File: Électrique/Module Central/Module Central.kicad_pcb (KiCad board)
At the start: 2 copper layers, 48.2 x 45.8 mm, 48 parts, among them J101 2.1mm X 5.5mm Barrel Connector, J102 Prog, J103 Conn_Coaxial, J201 USB_B_Mini, J301 Borne 0, J302 Borne 1, J303 Borne 2, J304 Borne 3, U101 LM2937xMP, U102 ATmega328P-AU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

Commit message: Ajout DEL témoin
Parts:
- added D105: TA, Diode_SMD:D_0805_2012Metric, F.Cu at (131.0, 44.8)
- added R106: 330, Resistor_SMD:R_0805_2012Metric, B.Cu at (131.8, 44.8)
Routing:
- net 5V: track 177.9 -> 182.5 mm
- net Net-(D105-Pad1): track 0.00 -> 4.53 mm, vias 0 -> 1

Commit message: Modification PCB prete à faire
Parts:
- added R201: 10K, Resistor_SMD:R_0805_2012Metric, F.Cu at (164.8, 35.5)
- added U104: FXMA108, Package_DFN_QFN:WQFN-20-1EP_2.5x4.5mm_P0.5mm_EP1x2.9mm, F.Cu at (149.2, 37.5)
- C203: value 0.01 -> 0.1
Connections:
- R102 pad 2: GND -> Net-(R102-Pad2)
- R103 pad 2: GND -> Net-(R103-Pad2)
- R104 pad 2: GND -> Net-(R104-Pad2)
- R105 pad 2: GND -> Net-(R105-Pad2)
- R106 pad 2: GND -> Net-(R106-Pad2)
- U102 pad 23: RX -> Net-(U102-Pad23)
- U102 pad 24: TX -> Net-(U102-Pad24)
- U102 pad 30: Net-(U102-Pad30) -> RX
- U102 pad 31: Net-(U102-Pad31) -> TX
- U102 pad 32: /D2 -> Net-(U102-Pad32)
- U103 pad 14: /D2 -> Net-(U103-Pad14)
- U103 pad 2: Net-(JP101-Pad2) -> Net-(U103-Pad2)
- U103 pad 3: Net-(JP102-Pad2) -> Net-(U103-Pad3)
- U103 pad 5: /D10 -> Net-(U103-Pad5)
- U103 pad 6: /D9 -> Net-(U103-Pad6)
- U201 pad 15: Net-(C201-Pad1) -> Net-(J201-Pad3)
- U201 pad 16: Net-(C202-Pad1) -> Net-(J201-Pad2)

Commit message: PCB modifié
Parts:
- removed C201, C202: 47p, Capacitor_SMD:C_0805_2012Metric
- removed the R201 at (125.2, 41.0)
- removed R202: 20, Resistor_SMD:R_0805_2012Metric
- R201, U104: moved to B.Cu
- moved R201 63.4 mm to (105.0, 56.8)
- moved U104 33.7 mm to (122.5, 58.0), turned to 90 degrees
- moved J103 0.50 mm to (108.2, 36.0)
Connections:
- R102 pad 2: Net-(R102-Pad2) -> GND
- R103 pad 2: Net-(R103-Pad2) -> GND
- R104 pad 2: Net-(R104-Pad2) -> GND
- R105 pad 2: Net-(R105-Pad2) -> GND
- R106 pad 2: Net-(R106-Pad2) -> GND
- U103 pad 4: /SCK_D13 -> Net-(U103-Pad4)
- U104 pad 14: Net-(U104-Pad14) -> Net-(U103-Pad4)
- U104 pad 7: Net-(U104-Pad7) -> /SCK_D13
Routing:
- net Net-(U103-Pad14): track 0.00 -> 22.2 mm, vias 0 -> 3
- net /D2: track 16.2 -> 0.00 mm
- net Net-(J201-Pad2): track 4.80 -> 20.1 mm
- net Net-(C202-Pad1): track 14.9 -> 0.00 mm
- net /D9: track 26.9 -> 12.1 mm, vias 2 -> 1
- net Net-(JP102-Pad2): track 20.8 -> 34.5 mm, vias 2 -> 3
- net Net-(U102-Pad32): track 0.00 -> 13.2 mm, vias 0 -> 3
- net Net-(U103-Pad6): track 0.00 -> 12.9 mm, vias 0 -> 1
- net GND: track 111.6 -> 124.1 mm, vias 11 -> 14
- net /D10: track 24.4 -> 12.4 mm, vias 2 -> 1
- net 5V: track 182.5 -> 193.6 mm
- net Net-(U103-Pad5): track 0.00 -> 10.5 mm, vias 0 -> 1
- net Net-(J201-Pad3): track 9.58 -> 19.9 mm
- net Net-(C201-Pad1): track 10.00 -> 0.00 mm
- net RX: track 11.0 -> 2.66 mm
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
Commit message: Modif PCB en cours
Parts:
- added JP103: Jumper, Connector_PinSocket_2.54mm:PinSocket_1x02_P2.54mm_Vertical, F.Cu at (147.2, 57.0)
- added JP104: Jumper, Connector_PinSocket_2.54mm:PinSocket_1x02_P2.54mm_Vertical, F.Cu at (151.8, 57.0)
- added R107: 1K, Resistor_SMD:R_0805_2012Metric, F.Cu at (147.1, 63.3)
- added R108: 1K, Resistor_SMD:R_0805_2012Metric, F.Cu at (151.5, 63.3)
- added U105: TXB0104RGY, Package_DFN_QFN:Texas_S-PVQFN-N14, B.Cu at (117.8, 58.0)
- U104: value FXMA108 -> TXB0104RGY; footprint Package_DFN_QFN:WQFN-20-1EP_2.5x4.5mm_P0.5mm_EP1x2.9mm -> Package_DFN_QFN:Texas_S-PVQFN-N14
- moved U104 0.25 mm to (122.8, 58.0), turned to 270 degrees
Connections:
- U104 pad 1: 5V -> 3V3
- U104 pad 10: GND -> Net-(U102-Pad32)
- U104 pad 11: GND -> Net-(JP101-Pad2)
- U104 pad 12: Net-(U104-Pad12) -> Net-(JP102-Pad2)
- U104 pad 13: Net-(U104-Pad13) -> /SCK_D13
- U104 pad 14: Net-(U103-Pad4) -> 5V
- U104 pad 15: Net-(U103-Pad6) -> GND
- U104 pad 2: Net-(U102-Pad32) -> Net-(U103-Pad4)
- U104 pad 3: Net-(JP101-Pad2) -> Net-(U103-Pad3)
- U104 pad 4: Net-(JP102-Pad2) -> Net-(U103-Pad2)
- U104 pad 5: /D10 -> Net-(U103-Pad14)
- U104 pad 6: /D9 -> Net-(U104-Pad6)
- U104 pad 7: /SCK_D13 -> GND
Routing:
- net Net-(U102-Pad32): track 13.2 -> 0.00 mm, vias 3 -> 0
- net DTR: track 31.3 -> 37.5 mm
- net Net-(U103-Pad14): track 22.2 -> 27.5 mm
- net Net-(JP102-Pad2): track 34.5 -> 30.7 mm
- net Net-(U103-Pad5): track 10.5 -> 13.8 mm
- net 3V3: track 45.8 -> 42.6 mm
- net GND: track 124.1 -> 121.8 mm, vias 14 -> 13
- net Net-(U103-Pad6): track 12.9 -> 14.9 mm
- net Net-(U103-Pad2): track 8.26 -> 10.0 mm
- net Net-(R203-Pad2): track 10.9 -> 12.6 mm
- net TX: track 16.5 -> 18.1 mm
- net 5V: track 193.6 -> 192.2 mm
- net /MOSI_D11: track 37.7 -> 39.0 mm
- net /D9: track 12.1 -> 13.3 mm
- net Net-(JP101-Pad2): track 26.4 -> 25.2 mm
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
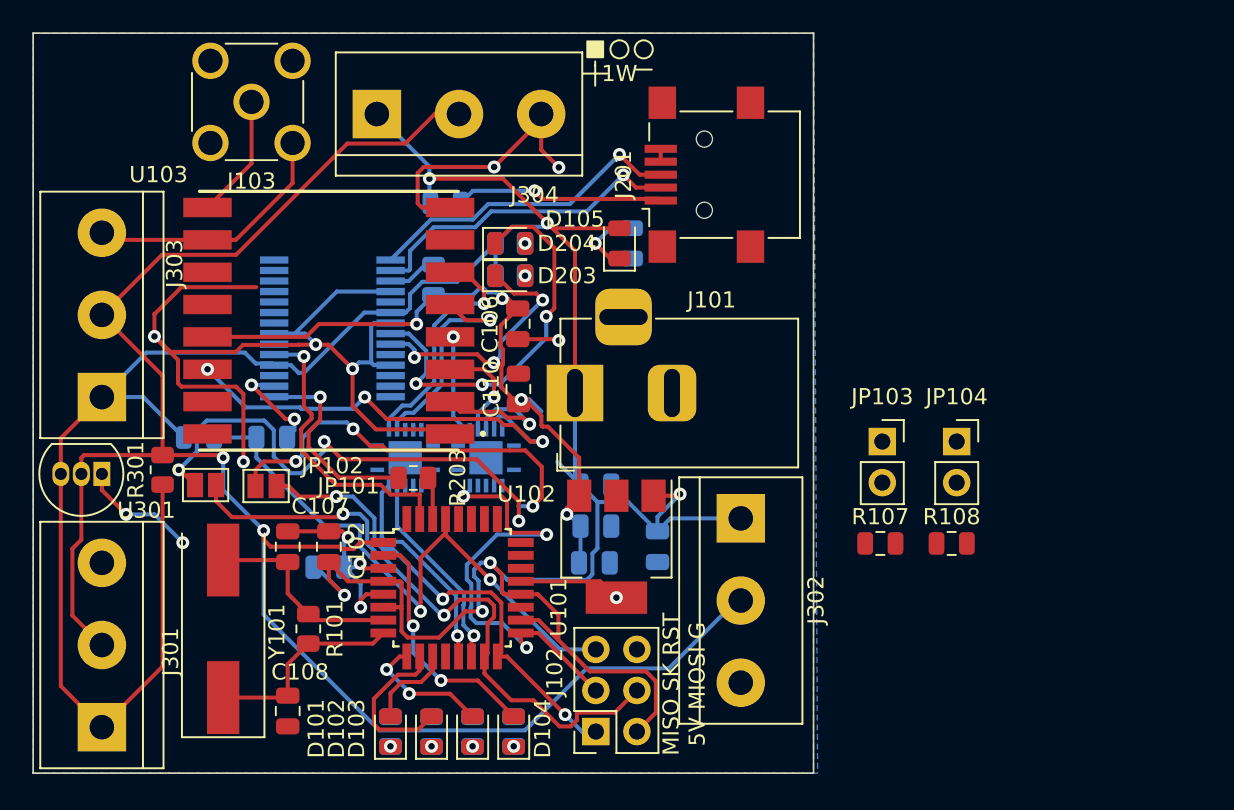
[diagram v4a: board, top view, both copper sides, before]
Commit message: PCB Avec 2x 4Channel LevelShifters
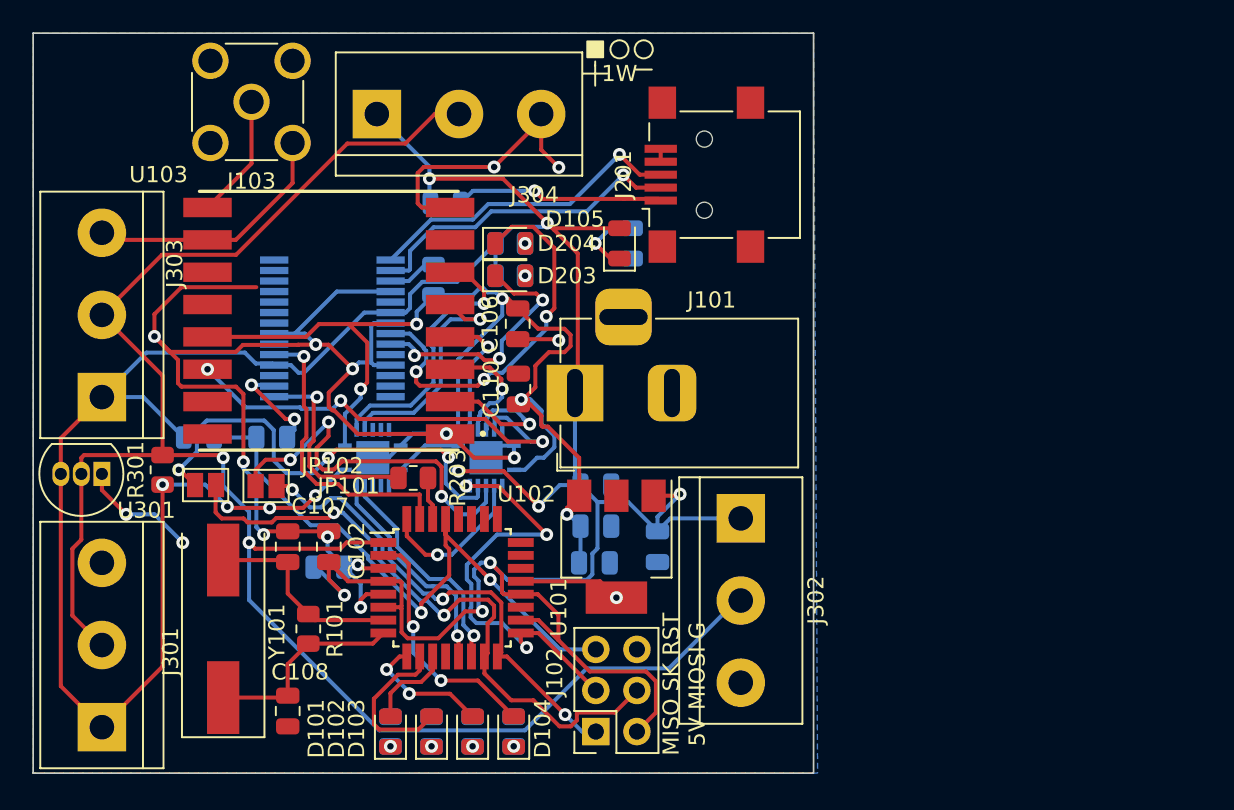
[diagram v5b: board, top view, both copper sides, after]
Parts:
- removed JP103, JP104: Jumper, Connector_PinSocket_2.54mm:PinSocket_1x02_P2.54mm_Vertical
- removed R107, R108: 1K, Resistor_SMD:R_0805_2012Metric
- moved U105 2.00 mm to (115.8, 58.0)
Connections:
- U104 pad 8: Net-(JP104-Pad1) -> 3V3
- U105 pad 8: Net-(JP103-Pad1) -> 3V3
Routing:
- net 3V3: track 42.6 -> 76.3 mm, vias 4 -> 5
- net GND: track 121.8 -> 142.3 mm, vias 13 -> 16
- net 5V: track 192.2 -> 212.3 mm, vias 6 -> 12
- net Net-(U102-Pad32): track 0.00 -> 9.67 mm, vias 0 -> 1
- net Net-(JP102-Pad2): track 30.7 -> 28.1 mm
- net Net-(U103-Pad6): track 14.9 -> 17.0 mm
- net Net-(U103-Pad4): track 6.30 -> 8.18 mm
- net /D10: track 12.6 -> 14.2 mm
- net Net-(JP101-Pad2): track 25.2 -> 24.2 mm
- net /SCK_D13: track 28.1 -> 27.1 mm
- net Net-(U103-Pad3): track 6.52 -> 7.52 mm
- net Net-(U103-Pad5): track 13.8 -> 14.7 mm
- net DTR: track 37.5 -> 38.4 mm
- net /D9: track 13.3 -> 13.9 mm
